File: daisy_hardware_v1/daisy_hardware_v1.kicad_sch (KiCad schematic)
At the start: 31 parts, among them J1 Conn_02x08_Odd_Even, J2 PJ398SM-12, J3 PJ398SM-12, J4 Connector_Audio:Jack_3.5mm_Qi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, J5 PJ398SM-12, SW1 SW_SPST, SW2 SW_SPST, U1 RAF_DAISY_SEED_V1, U2 TL072, U3 CD4051B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

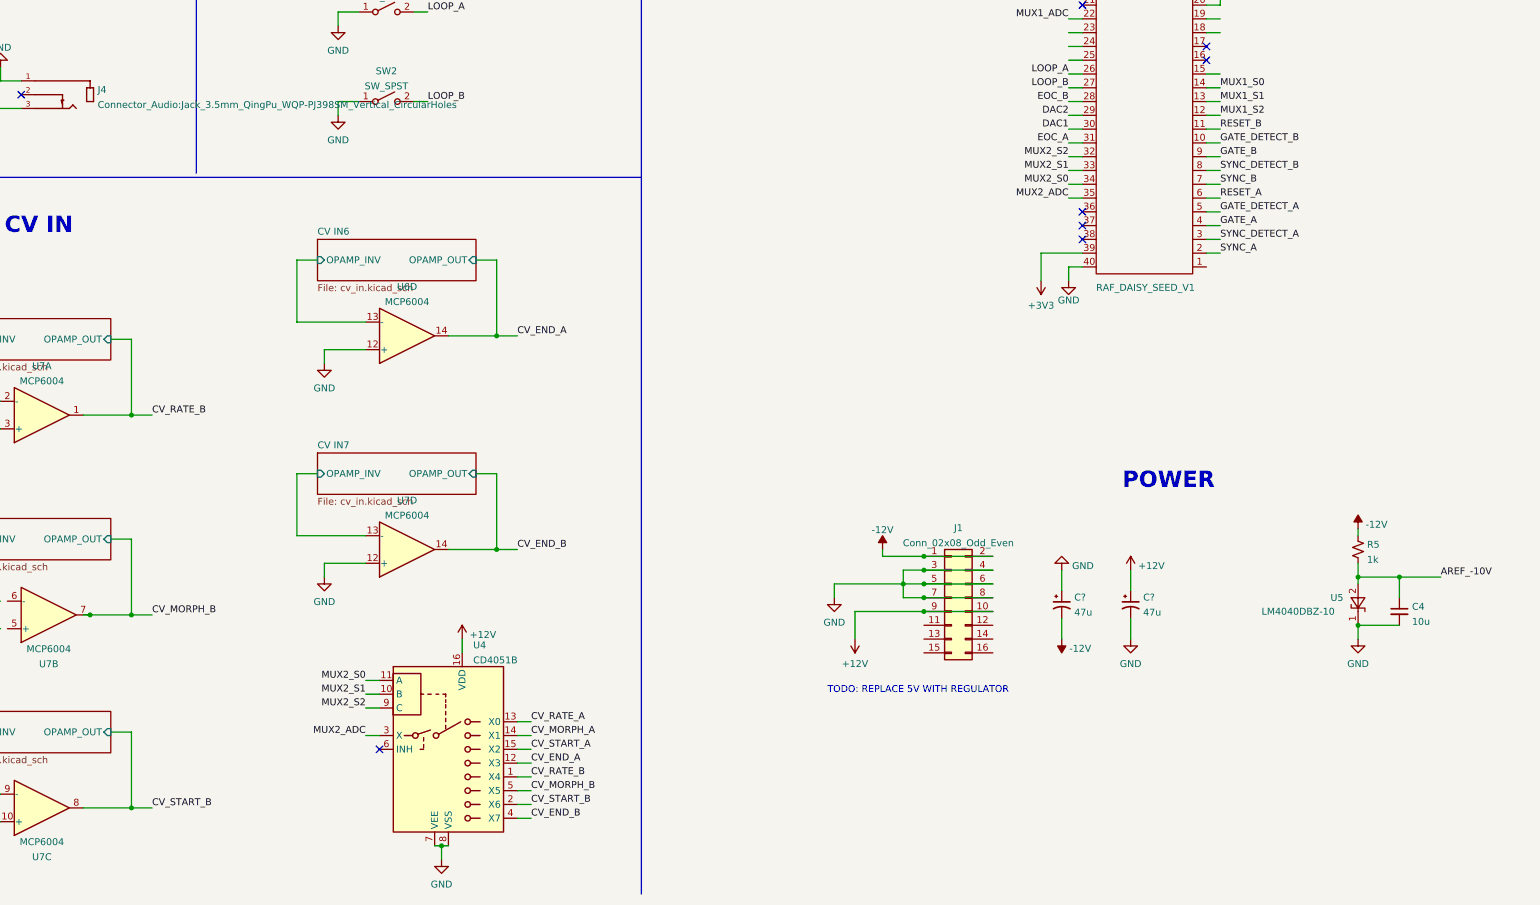
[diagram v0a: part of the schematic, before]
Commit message: Update power + add start/end to schematics
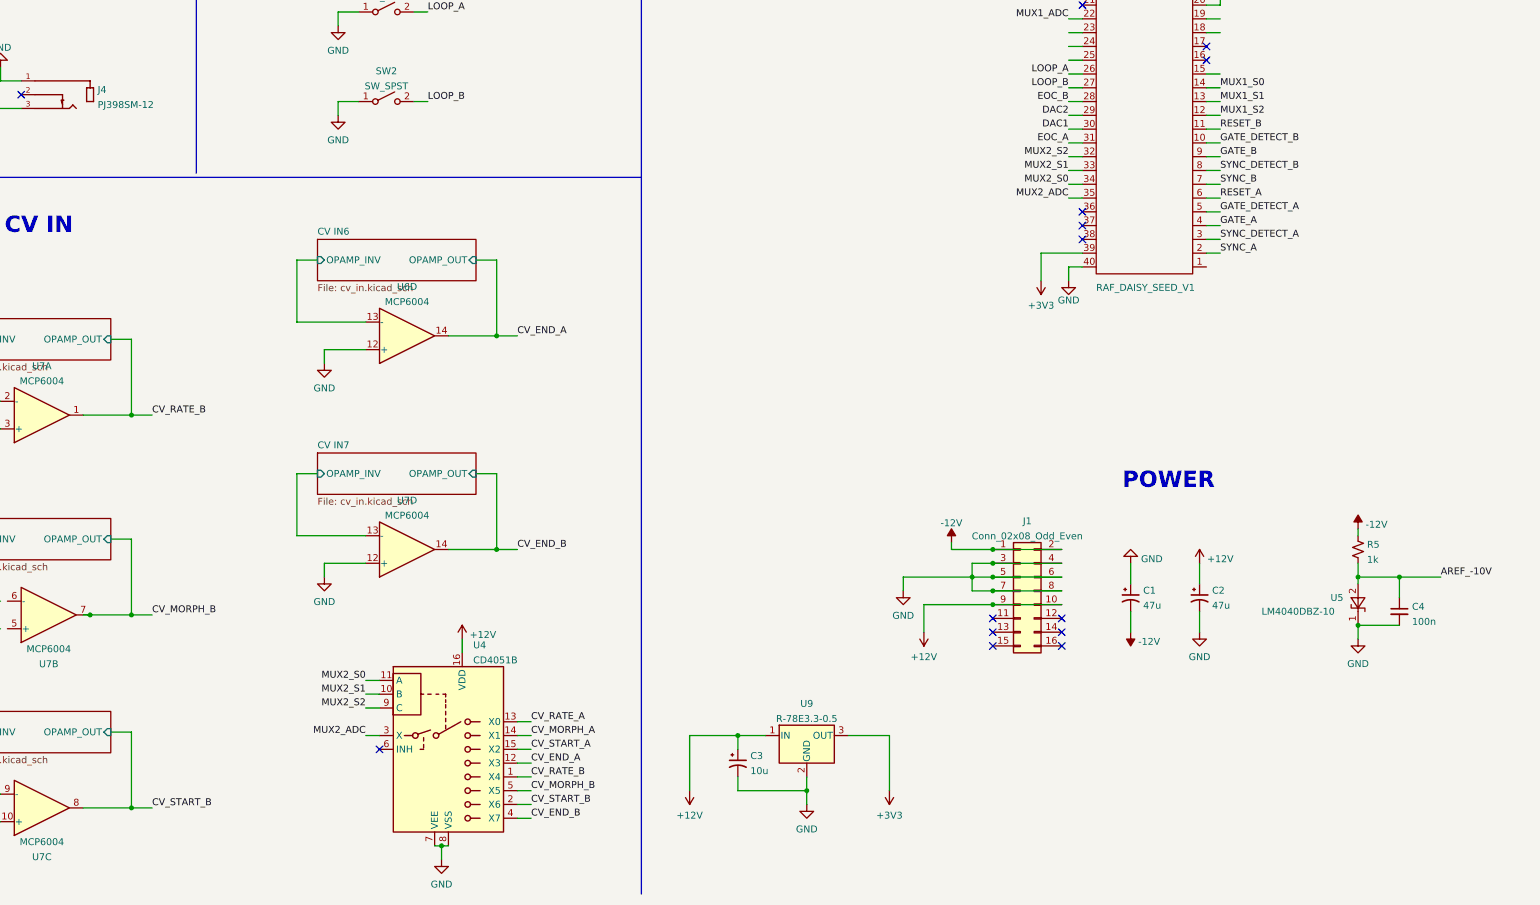
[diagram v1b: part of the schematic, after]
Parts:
- added C3: 10u, symbol Device:C_Polarized_Small_US
- added U9: R-78E3.3-0.5, Converter_DCDC:Converter_DCDC_RECOM_R-78E-0.5_THT, symbol Regulator_Switching:R-78E3.3-0.5
- C4: value 10u -> 100n
- J2, J3, J5: footprint Connector_Audio:Jack_3.5mm_QingPu_WQP-PJ398SM_Vertical_CircularHoles -> lowstepper_internal_footprint_lib:THONK_PJ398SM-12
- J4: value Connector_Audio:Jack_3.5mm_QingPu_WQP-PJ398SM_Vertical_CircularHoles -> PJ398SM-12; footprint Connector_Audio:Jack_3.5mm_QingPu_WQP-PJ398SM_Vertical_CircularHoles -> lowstepper_internal_footprint_lib:THONK_PJ398SM-12
- gave numbers to parts that had none: 2
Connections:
- net +12V: now also C3.1, U9.1 (IN)
- net +3V3: now also U9.3 (OUT)
- net GND: now also C3.2, U9.2 (GND)
- no-connect marks 14 -> 20
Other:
- note removed: "TODO: REPLACE 5V WITH REGULATOR"
- moved on the sheet: C1, C2, J1

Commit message: Start splitting up board
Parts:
- removed U3, U4: CD4051B, Package_DIP:DIP-16_W7.62mm, symbol Analog_Switch:CD4051B
- added J20, J21: Conn_01x16_Female, Connector_PinSocket_2.54mm:PinSocket_1x16_P2.54mm_Vertical, symbol Connector:Conn_01x16_Female
- added J6, J9: Conn_01x16_Male, Connector_PinHeader_2.54mm:PinHeader_1x16_P2.54mm_Vertical, symbol Connector:Conn_01x16_Male
- added U3, U4: 74HC4051, Package_SO:SOIC-16_3.9x9.9mm_P1.27mm, symbol 74xx:74HC4051
- C3: footprint (none) -> Capacitor_SMD:CP_Elec_3x5.3
- C4: footprint (none) -> Capacitor_SMD:C_0603_1608Metric
- R1, R2, R3, R4, R5: footprint (none) -> Resistor_SMD:R_0603_1608Metric
- SW1, SW2: footprint (none) -> Connector_PinSocket_2.54mm:PinSocket_1x03_P2.54mm_Vertical
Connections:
- net +12V: now also U3.16 (VCC), U4.16 (VCC)
- net CV_END_A: now also J20.7 (Pin_7), J6.7 (Pin_7), U4.12 (A3)
- net CV_END_B: now also J20.8 (Pin_8), J6.8 (Pin_8), U4.4 (A7)
- net CV_MORPH_A: now also J20.2 (Pin_2), J6.2 (Pin_2), U4.14 (A1)
- net CV_MORPH_B: now also J20.5 (Pin_5), J6.5 (Pin_5), U4.5 (A5)
- net CV_RATE_A: now also J20.1 (Pin_1), J6.1 (Pin_1), U4.13 (A0)
- net CV_RATE_B: now also J20.4 (Pin_4), J6.4 (Pin_4), U4.1 (A4)
- net CV_START_A: now also J20.3 (Pin_3), J6.3 (Pin_3), U4.15 (A2)
- net CV_START_B: now also J20.6 (Pin_6), J6.6 (Pin_6), U4.2 (A6)
- net GND: now also U3.6 (~{E}), U3.7 (VEE), U3.8 (GND), U4.6 (~{E}), U4.7 (VEE), U4.8 (GND)
- net LOOP_A: no longer SW1.2 (B)
- net LOOP_B: no longer SW2.2 (B)
- net MUX1_ADC: now also U3.3 (A)
- net MUX1_S0: now also U1.15, U3.11 (S0); no longer U1.14
- net MUX1_S1: now also U1.14, U3.10 (S1); no longer U1.13
- net MUX1_S2: now also U1.13, U3.9 (S2); no longer U1.12
- net MUX2_ADC: now also U4.3 (A)
- net MUX2_S0: now also U4.11 (S0)
- net MUX2_S1: now also U4.10 (S1)
- net MUX2_S2: now also U4.9 (S2)
- net POT_END_A: now also J9.7 (Pin_7)
- net POT_END_B: now also J9.8 (Pin_8)
- net POT_MORPH_A: now also J9.3 (Pin_3)
- net POT_MORPH_B: now also J9.4 (Pin_4)
- net POT_RATE_A: now also J9.2 (Pin_2)
- net POT_RATE_B: now also J9.1 (Pin_1)
- net POT_START_A: now also J9.5 (Pin_5)
- net POT_START_B: now also J9.6 (Pin_6)
- net RESET_A: now also J21.12 (Pin_12)
- net RESET_B: now also J21.16 (Pin_16)
- net SYNC_A: now also J21.10 (Pin_10)
- net SYNC_B: now also J21.14 (Pin_14)
- net SYNC_DETECT_A: now also J21.9 (Pin_9), J9.9 (Pin_9)
- net SYNC_DETECT_B: now also J21.13 (Pin_13), J9.13 (Pin_13)
- net EOC_B_BOTTOM: now reaches U8.1, U8.2 (-)
- net EOC_B_BOTTOM: now also J20.12 (Pin_12); no longer J5.3
- net DAC2_BOTTOM: now reaches R3.2, U2.7
- net DAC2_BOTTOM: now also J20.13 (Pin_13); no longer J2.3
- net DAC1_BOTTOM: now reaches R4.2, U2.1
- net DAC1_BOTTOM: now also J20.14 (Pin_14); no longer J3.3
- net EOC_A_BOTTOM: now reaches U8.6 (-), U8.7
- net EOC_A_BOTTOM: now also J20.11 (Pin_11); no longer J4.3
- net GATE_A: no longer names the net of U1.4
- net GATE_B: no longer names the net of U1.9
- net GATE_DETECT_A renamed RESET_DETECT_A
- net RESET_DETECT_A: now also J21.11 (Pin_11), J9.11 (Pin_11)
- net GATE_DETECT_B renamed RESET_DETECT_B
- net RESET_DETECT_B: now also J21.15 (Pin_15), J9.15 (Pin_15)
- new net DAC1_TOP: J3.3, J6.14 (Pin_14)
- new net DAC2_TOP: J2.3, J6.13 (Pin_13)
- new net EOC_A_TOP: J4.3, J6.11 (Pin_11)
- new net EOC_B_TOP: J5.3, J6.12 (Pin_12)
- new net POT_END_A_BOTTOM: J21.7 (Pin_7), U3.2 (A6)
- new net POT_END_B_BOTTOM: J21.8 (Pin_8), U3.4 (A7)
- new net POT_MORPH_A_BOTTOM: J21.3 (Pin_3), U3.15 (A2)
- new net POT_MORPH_B_BOTTOM: J21.4 (Pin_4), U3.12 (A3)
- new net POT_RATE_A_BOTTOM: J21.2 (Pin_2), U3.14 (A1)
- new net POT_RATE_B_BOTTOM: J21.1 (Pin_1), U3.13 (A0)
- new net POT_START_A_BOTTOM: J21.5 (Pin_5), U3.1 (A4)
- new net POT_START_B_BOTTOM: J21.6 (Pin_6), U3.5 (A5)
- new net RESET_A_TOP: J9.12 (Pin_12)
- new net RESET_B_TOP: J9.16 (Pin_16)
- new net SW_A_BOTTOM: J20.9 (Pin_9)
- new net SW_A_TOP: J6.9 (Pin_9), SW1.2 (B)
- new net SW_B_BOTTOM: J20.10 (Pin_10)
- new net SW_B_TOP: J6.10 (Pin_10), SW2.2 (B)
- new net SYNC_A_TOP: J9.10 (Pin_10)
- new net SYNC_B_TOP: J9.14 (Pin_14)
- no-connect marks 20 -> 16
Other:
- removed sheet Gate In
- removed sheet Gate In3
- sheet Gate In1 ports: added INPUT_BOTTOM, INPUT_TOP; removed none
- sheet Gate In2 ports: added INPUT_BOTTOM, INPUT_TOP; removed none
- sheet Gate In4 ports: added INPUT_BOTTOM, INPUT_TOP; removed none
- sheet Gate In5 ports: added INPUT_BOTTOM, INPUT_TOP; removed none
- moved on the sheet: C1, C2, C3, C4, J1, J2, J3, J4, J5, R1, R2, R3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

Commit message: Almost done PCB
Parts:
- U1: footprint (none) -> lowstepper_internal_footprint_lib:DAISY_SEED_OKAYSYNTH
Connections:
- net CV IN3/OPAMP_INV: now also U7.6 (-)
- net CV_END_A: no longer J20.7 (Pin_7)
- net CV_END_B: no longer J20.8 (Pin_8)
- net CV_MORPH_A: no longer J20.2 (Pin_2)
- net CV_MORPH_B: no longer J20.5 (Pin_5)
- net CV_RATE_A: no longer J20.1 (Pin_1)
- net CV_RATE_B: no longer J20.4 (Pin_4)
- net CV_START_A: no longer J20.3 (Pin_3)
- net CV_START_B: no longer J20.6 (Pin_6)
- net DAC1_BOTTOM: now also J21.3 (Pin_3); no longer J20.14 (Pin_14)
- net DAC1_TOP: now also J9.3 (Pin_3); no longer J6.14 (Pin_14)
- net DAC2_BOTTOM: now also J21.4 (Pin_4); no longer J20.13 (Pin_13)
- net DAC2_TOP: now also J9.4 (Pin_4); no longer J6.13 (Pin_13)
- net EOC_A_BOTTOM: now also J21.5 (Pin_5); no longer J20.11 (Pin_11)
- net EOC_A_TOP: now also J9.5 (Pin_5); no longer J6.11 (Pin_11)
- net EOC_B_BOTTOM: now also J21.6 (Pin_6); no longer J20.12 (Pin_12)
- net EOC_B_TOP: now also J9.6 (Pin_6); no longer J6.12 (Pin_12)
- net GND: now also U7.5 (+)
- net MUX1_S0: now also U1.7; no longer U1.15
- net MUX1_S1: now also U1.6; no longer U1.14
- net MUX1_S2: now also U1.5; no longer U1.13
- net POT_END_A: now also J6.15 (Pin_15); no longer J9.7 (Pin_7)
- net POT_END_A_BOTTOM: now also J20.15 (Pin_15); no longer J21.7 (Pin_7)
- net POT_END_B: now also J6.16 (Pin_16); no longer J9.8 (Pin_8)
- net POT_END_B_BOTTOM: now also J20.16 (Pin_16); no longer J21.8 (Pin_8)
- net POT_MORPH_A: now also J6.11 (Pin_11); no longer J9.3 (Pin_3)
- net POT_MORPH_A_BOTTOM: now also J20.9 (Pin_9); no longer J21.3 (Pin_3)
- net POT_MORPH_B: now also J6.12 (Pin_12); no longer J9.4 (Pin_4)
- net POT_MORPH_B_BOTTOM: now also J20.12 (Pin_12); no longer J21.4 (Pin_4)
- net POT_RATE_A: now also J6.10 (Pin_10); no longer J9.2 (Pin_2)
- net POT_RATE_A_BOTTOM: now also J20.10 (Pin_10); no longer J21.2 (Pin_2)
- net POT_RATE_B: now also J6.9 (Pin_9); no longer J9.1 (Pin_1)
- net POT_RATE_B_BOTTOM: now also J20.11 (Pin_11); no longer J21.1 (Pin_1)
- net POT_START_A: now also J6.13 (Pin_13); no longer J9.5 (Pin_5)
- net POT_START_A_BOTTOM: now also J20.13 (Pin_13); no longer J21.5 (Pin_5)
- net POT_START_B: now also J6.14 (Pin_14); no longer J9.6 (Pin_6)
- net POT_START_B_BOTTOM: now also J20.14 (Pin_14); no longer J21.6 (Pin_6)
- net RESET_A: now also U1.14; no longer J21.12 (Pin_12), U1.6
- net RESET_A_BOTTOM: now also J21.15 (Pin_15)
- net RESET_A_TOP: now also J9.15 (Pin_15); no longer J9.12 (Pin_12)
- net RESET_B: now also U1.15; no longer J21.16 (Pin_16), U1.11
- net RESET_B_BOTTOM: now also J21.16 (Pin_16)
- net RESET_DETECT_A: now also J21.10 (Pin_10), J9.10 (Pin_10), U1.2; no longer J21.11 (Pin_11), J9.11 (Pin_11), U1.5
- net RESET_DETECT_B: now also J21.12 (Pin_12), J9.12 (Pin_12); no longer J21.15 (Pin_15), J9.15 (Pin_15)
- net SW_A_BOTTOM: now also J21.1 (Pin_1); no longer J20.9 (Pin_9)
- net SW_A_TOP: now also J9.1 (Pin_1); no longer J6.9 (Pin_9)
- net SW_B_BOTTOM: now also J21.2 (Pin_2); no longer J20.10 (Pin_10)
- net SW_B_TOP: now also J9.2 (Pin_2); no longer J6.10 (Pin_10)
- net SYNC_A: now also U1.13; no longer J21.10 (Pin_10), U1.2
- net SYNC_A_BOTTOM: now also J21.13 (Pin_13)
- net SYNC_A_TOP: now also J9.13 (Pin_13); no longer J9.10 (Pin_10)
- net SYNC_B: now also U1.11; no longer J21.14 (Pin_14), U1.7
- net SYNC_DETECT_B: now also J21.11 (Pin_11), J9.11 (Pin_11), U1.9; no longer J21.13 (Pin_13), J9.13 (Pin_13), U1.8
- new net CV_END_A_BOTTOM: J20.3 (Pin_3)
- new net CV_END_B_BOTTOM: J20.7 (Pin_7)
- new net CV_MORPH_A_BOTTOM: J20.1 (Pin_1)
- new net CV_MORPH_B_BOTTOM: J20.5 (Pin_5)
- new net CV_RATE_A_BOTTOM: J20.2 (Pin_2)
- new net CV_RATE_B_BOTTOM: J20.6 (Pin_6)
- new net CV_START_A_BOTTOM: J20.4 (Pin_4)
- new net CV_START_B_BOTTOM: J20.8 (Pin_8)
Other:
- sheet CV IN ports: added JACK_BOTTOM, JACK_TOP; removed none
- sheet CV IN1 ports: added JACK_BOTTOM, JACK_TOP; removed none
- sheet CV IN2 ports: added JACK_BOTTOM, JACK_TOP; removed none
- sheet CV IN3 ports: added JACK_BOTTOM, JACK_TOP; removed none
- sheet CV IN4 ports: added JACK_BOTTOM, JACK_TOP; removed none
- sheet CV IN5 ports: added JACK_BOTTOM, JACK_TOP; removed none
- sheet CV IN6 ports: added JACK_BOTTOM, JACK_TOP; removed none
- sheet CV IN7 ports: added JACK_BOTTOM, JACK_TOP; removed none
- moved on the sheet: U6A, U6C, U6D, U6E, U7A, U7B, U7C, U7D, U7E

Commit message: p much done bottom board
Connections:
- net +12V: no longer U3.16 (VCC), U4.16 (VCC)
- net +3V3: now also U3.16 (VCC), U4.16 (VCC)
- net CV_END_A: now also U4.2 (A6); no longer U4.12 (A3)
- net CV_END_B: now also U4.13 (A0); no longer U4.4 (A7)
- net CV_MORPH_A: now also U4.5 (A5); no longer U4.14 (A1)
- net CV_MORPH_B: now also U4.14 (A1); no longer U4.5 (A5)
- net CV_RATE_A: now also U4.4 (A7); no longer U4.13 (A0)
- net CV_RATE_B: now also U4.15 (A2); no longer U4.1 (A4)
- net CV_START_A: now also U4.1 (A4); no longer U4.15 (A2)
- net CV_START_B: now also U4.12 (A3); no longer U4.2 (A6)
- net DAC1: now also U1.29; no longer U1.30
- net DAC2: now also U1.30; no longer U1.29
- net EOC_A: now also U1.27; no longer U1.31
- net EOC_B: now also U1.26; no longer U1.28
- net LOOP_A: now also U1.24; no longer U1.26
- net LOOP_B: now also U1.25; no longer U1.27
- net MUX1_ADC: now also U1.35; no longer U1.22
- net MUX1_S0: now also U1.34; no longer U1.7
- net MUX1_S1: now also U1.33; no longer U1.6
- net MUX1_S2: now also U1.32; no longer U1.5
- net MUX2_ADC: now also U1.31; no longer U1.35
- net MUX2_S0: now also U1.4; no longer U1.34
- net MUX2_S1: now also U1.3; no longer U1.33
- net MUX2_S2: now also U1.2; no longer U1.32
- net RESET_DETECT_A: now also U1.9; no longer U1.2
- net RESET_DETECT_B: now also U1.7; no longer U1.10
- net SYNC_DETECT_A: now also U1.10; no longer U1.3
- net SYNC_DETECT_B: now also U1.8; no longer U1.9

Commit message: SPDT footprint
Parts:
- removed SW1, SW2: SW_SPST, Connector_PinSocket_2.54mm:PinSocket_1x03_P2.54mm_Vertical, symbol Switch:SW_SPST
- added SW? (x2): SW_SPDT, lowstepper_internal_footprint_lib:dailywell_sw_spdt, symbol Switch:SW_SPDT
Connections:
- net SW_A_BOTTOM is gone; now on net SW_A_1: J21.1 (Pin_1)
- net SW_B_BOTTOM is gone; now on net SW_A_2: J21.2 (Pin_2)
- net GND: now also SW?.2 (B), SW?.2 (B)
- net SYNC_B_BOTTOM: now also J21.14 (Pin_14)
- net SW_B_2: now reaches U1.22
- net SW_B_2: now also J21.8 (Pin_8)
- net SW_B_1: now reaches U1.23
- net SW_B_1: now also J21.7 (Pin_7)
- net SW_B_1_TOP: now reaches J9.7 (Pin_7)
- net SW_B_1_TOP: now also SW?.1 (A)
- net SW_B_2_TOP: now reaches J9.8 (Pin_8)
- net SW_B_2_TOP: now also SW?.3 (C)
- net LOOP_A renamed SW_A_2
- net LOOP_B renamed SW_A_1
- net SW_A_TOP renamed SW_A_1_TOP
- net SW_A_1_TOP: now also SW?.1 (A)
- net SW_B_TOP renamed SW_A_2_TOP
- net SW_A_2_TOP: now also SW?.3 (C)

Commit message: board connectors expanded
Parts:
- removed J20, J21: Conn_01x16_Female, Connector_PinSocket_2.54mm:PinSocket_1x16_P2.54mm_Vertical, symbol Connector:Conn_01x16_Female
- removed J6, J9: Conn_01x16_Male, Connector_PinHeader_2.54mm:PinHeader_1x16_P2.54mm_Vertical, symbol Connector:Conn_01x16_Male
- added C13: 10u, Capacitor_SMD:CP_Elec_3x5.3, symbol Device:C_Polarized_Small_US
- added J20, J21: Conn_01x18_Female, Connector_PinSocket_2.54mm:PinSocket_1x18_P2.54mm_Vertical, symbol Connector:Conn_01x18_Female
- added J6, J9: Conn_01x18_Male, Connector_PinHeader_2.54mm:PinHeader_1x18_P2.54mm_Vertical, symbol Connector:Conn_01x18_Male
- gave numbers to parts that had none: 2
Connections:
- net +3V3: now also J21.1 (Pin_1), J9.18 (Pin_18)
- net CV_END_A_BOTTOM: now also J20.15 (Pin_15)
- net CV_END_A_TOP: now also J6.8 (Pin_8)
- net CV_END_B_BOTTOM: now also J20.11 (Pin_11)
- net CV_END_B_TOP: now also J6.9 (Pin_9)
- net CV_MORPH_A_BOTTOM: now also J20.17 (Pin_17)
- net CV_MORPH_A_TOP: now also J6.3 (Pin_3)
- net CV_MORPH_B_BOTTOM: now also J20.13 (Pin_13)
- net CV_MORPH_B_TOP: now also J6.6 (Pin_6)
- net CV_RATE_A_BOTTOM: now also J20.16 (Pin_16)
- net CV_RATE_A_TOP: now also J6.2 (Pin_2)
- net CV_RATE_B_BOTTOM: now also J20.12 (Pin_12)
- net CV_RATE_B_TOP: now also J6.5 (Pin_5)
- net CV_START_A_BOTTOM: now also J20.14 (Pin_14)
- net CV_START_A_TOP: now also J6.4 (Pin_4)
- net CV_START_B_BOTTOM: now also J20.10 (Pin_10)
- net CV_START_B_TOP: now also J6.7 (Pin_7)
- net DAC1_BOTTOM: now also J21.15 (Pin_15)
- net DAC1_TOP: now also J9.4 (Pin_4)
- net DAC2_BOTTOM: now also J21.14 (Pin_14)
- net DAC2_TOP: now also J9.5 (Pin_5)
- net EOC_A_BOTTOM: now also J21.13 (Pin_13)
- net EOC_A_TOP: now also J9.6 (Pin_6)
- net EOC_B_BOTTOM: now also J21.12 (Pin_12)
- net EOC_B_TOP: now also J9.7 (Pin_7)
- net GND: now also C13.2, J21.18 (Pin_18), J9.1 (Pin_1)
- net POT_END_A_BOTTOM: now also J20.3 (Pin_3)
- net POT_END_B_BOTTOM: now also J20.2 (Pin_2)
- net POT_MORPH_A_BOTTOM: now also J20.9 (Pin_9)
- net POT_MORPH_B_BOTTOM: now also J20.6 (Pin_6)
- net POT_RATE_A_BOTTOM: now also J20.8 (Pin_8)
- net POT_RATE_B_BOTTOM: now also J20.7 (Pin_7)
- net POT_START_A_BOTTOM: now also J20.5 (Pin_5)
- net POT_START_B_BOTTOM: now also J20.4 (Pin_4)
- net RESET_A_BOTTOM: now also J21.2 (Pin_2)
- net RESET_A_TOP: now also J9.17 (Pin_17)
- net RESET_B_BOTTOM: now also J21.3 (Pin_3)
- net RESET_B_TOP: now also J9.16 (Pin_16)
- net SW_A_1_TOP: now also J9.2 (Pin_2)
- net SW_A_2_TOP: now also J9.3 (Pin_3)
- net SW_B_1_TOP: now also J9.8 (Pin_8)
- net SW_B_2_TOP: now also J9.9 (Pin_9)
- net SYNC_A_BOTTOM: now also J21.5 (Pin_5)
- net SYNC_A_TOP: now also J9.14 (Pin_14)
- net SYNC_B_BOTTOM: now also J21.4 (Pin_4)
- net SYNC_B_TOP: now also J9.15 (Pin_15)
- net +5V: now reaches J1.11 (Pin_11)
- net +5V: now also J1.12 (Pin_12), C13.1
- net POT_END_A renamed POT_END_A_TOP
- net POT_END_A_TOP: now also J6.16 (Pin_16)
- net POT_END_B renamed POT_END_B_TOP
- net POT_END_B_TOP: now also J6.17 (Pin_17)
- net POT_MORPH_A renamed POT_MORPH_A_TOP
- net POT_MORPH_A_TOP: now also J6.12 (Pin_12)
- net POT_MORPH_B renamed POT_MORPH_B_TOP
- net POT_MORPH_B_TOP: now also J6.13 (Pin_13)
- net POT_RATE_A renamed POT_RATE_A_TOP
- net POT_RATE_A_TOP: now also J6.11 (Pin_11)
- net POT_RATE_B renamed POT_RATE_B_TOP
- net POT_RATE_B_TOP: now also J6.10 (Pin_10)
- net POT_START_A renamed POT_START_A_TOP
- net POT_START_A_TOP: now also J6.14 (Pin_14)
- net POT_START_B renamed POT_START_B_TOP
- net POT_START_B_TOP: now also J6.15 (Pin_15)
- net RESET_DETECT_A renamed RESET_DETECT_A_BOTTOM
- net RESET_DETECT_A_BOTTOM: now also J21.8 (Pin_8)
- net RESET_DETECT_B renamed RESET_DETECT_B_BOTTOM
- net RESET_DETECT_B_BOTTOM: now also J21.6 (Pin_6)
- net SW_A_1 renamed SW_A_1_BOTTOM
- net SW_A_1_BOTTOM: now also J21.17 (Pin_17)
- net SW_A_2 renamed SW_A_2_BOTTOM
- net SW_A_2_BOTTOM: now also J21.16 (Pin_16)
- net SW_B_1 renamed SW_B_1_BOTTOM
- net SW_B_1_BOTTOM: now also J21.11 (Pin_11)
- net SW_B_2 renamed SW_B_2_BOTTOM
- net SW_B_2_BOTTOM: now also J21.10 (Pin_10)
- net SYNC_DETECT_A renamed SYNC_DETECT_A_BOTTOM
- net SYNC_DETECT_A_BOTTOM: now also J21.9 (Pin_9)
- net SYNC_DETECT_B renamed SYNC_DETECT_B_BOTTOM
- net SYNC_DETECT_B_BOTTOM: now also J21.7 (Pin_7)
- new net RESET_DETECT_A_TOP: J9.11 (Pin_11)
- new net RESET_DETECT_B_TOP: J9.13 (Pin_13)
- new net SYNC_DETECT_A_TOP: J9.10 (Pin_10)
- new net SYNC_DETECT_B_TOP: J9.12 (Pin_12)
- no-connect marks 16 -> 14
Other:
- sheet Gate In1 ports: added DETECT_BOTTOM, DETECT_TOP; removed DETECT
- sheet Gate In2 ports: added DETECT_BOTTOM, DETECT_TOP; removed DETECT
- sheet Gate In4 ports: added DETECT_BOTTOM, DETECT_TOP; removed DETECT
- sheet Gate In5 ports: added DETECT_BOTTOM, DETECT_TOP; removed DETECT
- moved on the sheet: C4, R5, U5
